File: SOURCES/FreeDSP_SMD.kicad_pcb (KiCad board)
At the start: 2 copper layers, 100 x 100 mm, 169 parts, among them IC1 AD8608, IC2 ADAU1701, IC3 24AA256, IC4 TC7SZ08, IC5 AD8608ARZ, IC6 AD8608, P1 CONN_02X11, P10 CONN_02X10, P2 CONN_2, P3 CONN_02X02, P4 USBi, P5 CONN_02X13, P6 CONN_01X06, P7 CONN_01X06, P8 CONN_01X06, P9 CONN_02X10, Q1 ZXTP25040DFHTA, Q2 2N7000, Q3 2N7000, U1 78033, U2 4040, U3 7805, X1 12M288Hz

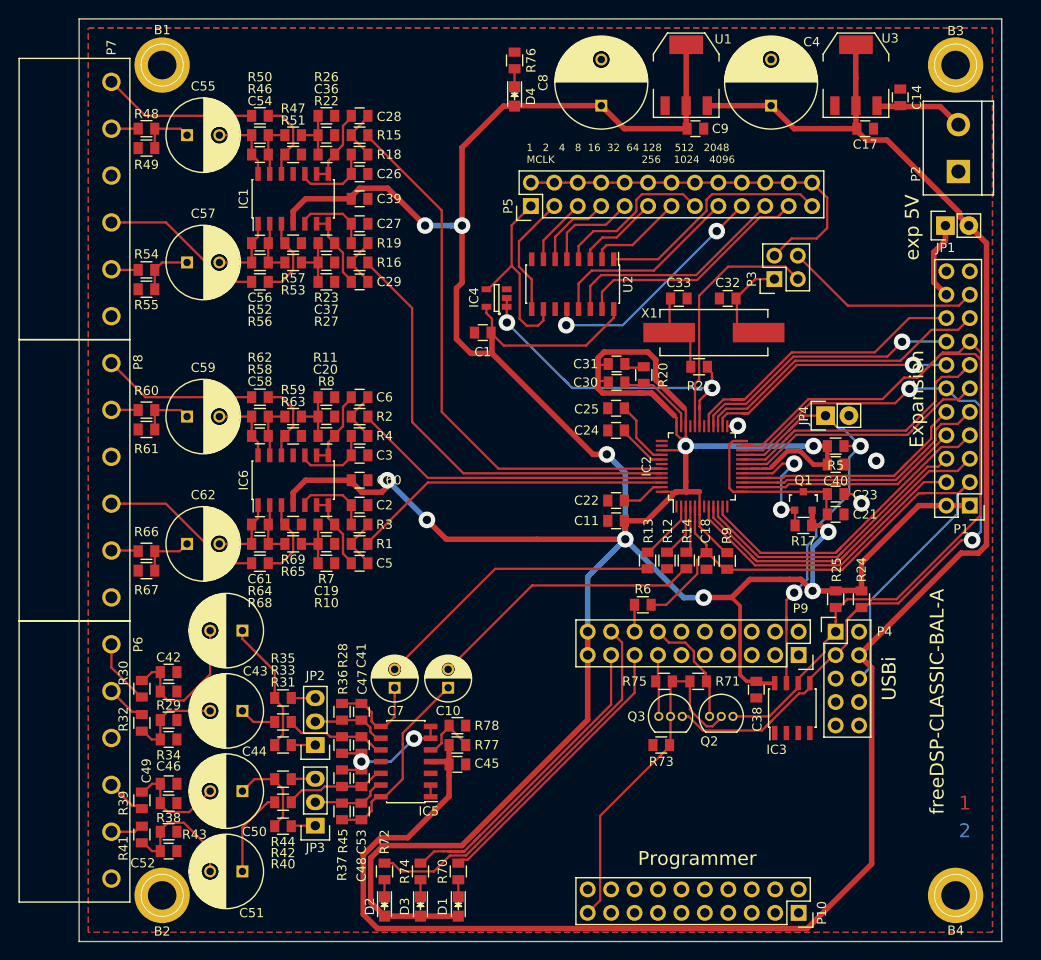
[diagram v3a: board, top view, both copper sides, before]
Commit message: Bugfix DAC-Stage: Applied VCC/2 - Supplied OpAmps with +5V - Reworked gain settings: Pro +6dBu, Consumer -10dBV
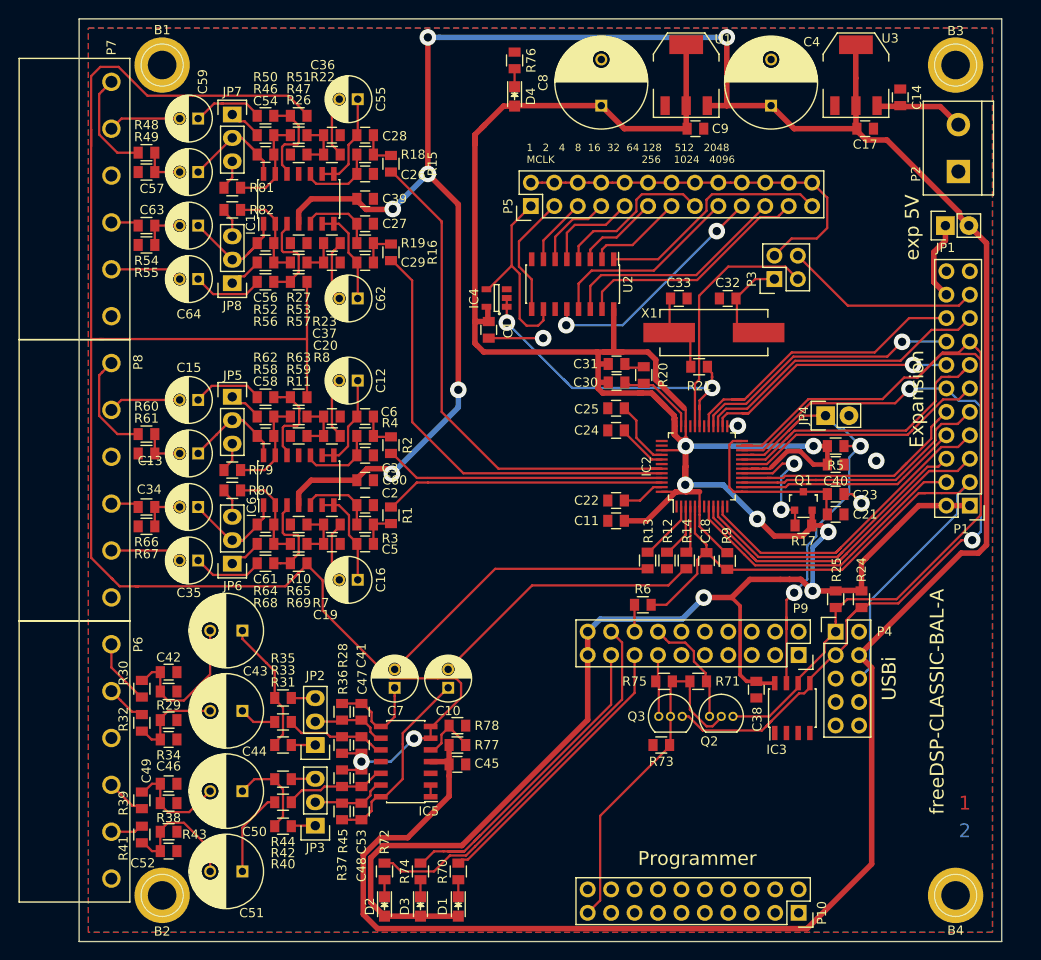
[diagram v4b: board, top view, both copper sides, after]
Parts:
- added C12: 47u0./16V, Capacitors_ThroughHole:C_Radial_D5_L11_P2, F.Cu at (130.2, 89.2)
- added C13: 47u0./16V, Capacitors_ThroughHole:C_Radial_D5_L11_P2, F.Cu at (112.9, 97.1)
- added C15: 47u0./16V, Capacitors_ThroughHole:C_Radial_D5_L11_P2, F.Cu at (112.9, 91.3)
- added C16: 47u0./16V, Capacitors_ThroughHole:C_Radial_D5_L11_P2, F.Cu at (130.2, 110.8)
- added C34: 47u0./16V, Capacitors_ThroughHole:C_Radial_D5_L11_P2, F.Cu at (112.9, 102.9)
- added C35: 47u0./16V, Capacitors_ThroughHole:C_Radial_D5_L11_P2, F.Cu at (112.9, 108.7)
- added C63: 47u0./16V, Capacitors_ThroughHole:C_Radial_D5_L11_P2, F.Cu at (112.9, 72.4)
- added C64: 47u0./16V, Capacitors_ThroughHole:C_Radial_D5_L11_P2, F.Cu at (112.9, 78.2)
- added JP5: JUMPER3, Pin_Headers:Pin_Header_Straight_1x03, F.Cu at (116.6, 91.0)
- added JP6: JUMPER3, Pin_Headers:Pin_Header_Straight_1x03, F.Cu at (116.6, 109.0)
- added JP7: JUMPER3, Pin_Headers:Pin_Header_Straight_1x03, F.Cu at (116.6, 60.4)
- added JP8: JUMPER3, Pin_Headers:Pin_Header_Straight_1x03, F.Cu at (116.6, 78.6)
- added R79: 17K4, rklib:C0805-RES, F.Cu at (116.6, 98.9)
- added R80: 17K4, rklib:C0805-RES, F.Cu at (116.6, 101.1)
- added R81: 17K4, rklib:C0805-RES, F.Cu at (116.6, 68.3)
- added R82: 17K4, rklib:C0805-RES, F.Cu at (116.6, 70.7)
- C55, C57, C59, C62: value 47u0 ./ 35V -> 47u0./16V; footprint Capacitors_ThroughHole:C_Radial_D8_L11.5_P3.5 -> Capacitors_ThroughHole:C_Radial_D5_L11_P2
- IC1, IC6: value AD8608 -> AD8608ARZ
- R10, R11: value 47K0 -> 49K9
- R46, R52, R58, R64: value 10K0 -> 3K57
- R7, R8: value 680R -> 604R
- moved C62 32.4 mm to (130.2, 80.3), turned to 180 degrees
- moved C59 32.3 mm to (112.9, 60.8), turned to 180 degrees
- moved C55 18.9 mm to (130.2, 58.7), turned to 180 degrees
- moved C57 9.87 mm to (112.9, 66.6), turned to 180 degrees
- moved R10 5.16 mm to (123.8, 104.8), turned to 180 degrees
- moved R11 5.16 mm to (123.8, 95.2), turned to 180 degrees
- moved R26 5.16 mm to (123.8, 64.7), turned to 180 degrees
- moved R27 5.16 mm to (123.8, 74.3), turned to 180 degrees
- moved R54 4.80 mm to (107.3, 72.4)
- moved R55 4.80 mm to (107.3, 74.5)
- moved R66 4.80 mm to (107.3, 102.9)
- moved R67 4.80 mm to (107.3, 105.0)
- moved R1 4.60 mm to (133.8, 103.8), turned to 90 degrees
- moved R2 4.60 mm to (133.8, 96.2), turned to 270 degrees
- moved R15 4.60 mm to (133.8, 65.7), turned to 270 degrees
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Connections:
- C39 pad 2: 3V3 -> +5V
- C5 pad 1: Net-(C5-Pad1) -> Net-(C16-Pad1)
- C55 pad 1: Net-(C55-Pad1) -> Net-(C28-Pad1)
- C55 pad 2: Net-(C54-Pad1) -> Net-(C55-Pad2)
- C57 pad 1: Net-(C57-Pad1) -> Net-(C54-Pad1)
- C57 pad 2: Net-(C56-Pad1) -> Net-(C57-Pad2)
- C58 pad 1: Net-(C58-Pad1) -> Net-(C13-Pad1)
- C59 pad 2: Net-(C58-Pad1) -> /OUT1-
- C6 pad 1: Net-(C6-Pad1) -> Net-(C12-Pad1)
- C60 pad 2: 3V3 -> +5V
- C61 pad 1: Net-(C61-Pad1) -> Net-(C34-Pad1)
- C62 pad 1: Net-(C62-Pad1) -> Net-(C29-Pad1)
- C62 pad 2: Net-(C61-Pad1) -> Net-(C62-Pad2)
- IC1 pad 4: 3V3 -> +5V
- IC6 pad 1: Net-(C61-Pad1) -> Net-(C34-Pad1)
- IC6 pad 14: Net-(C58-Pad1) -> Net-(C13-Pad1)
- IC6 pad 4: 3V3 -> +5V
- IC6 pad 6: Net-(C5-Pad1) -> Net-(C16-Pad1)
- IC6 pad 7: Net-(C5-Pad1) -> Net-(C16-Pad1)
- IC6 pad 8: Net-(C6-Pad1) -> Net-(C12-Pad1)
- IC6 pad 9: Net-(C6-Pad1) -> Net-(C12-Pad1)
- P10 pad 1: /PD3 -> (no net)
- P10 pad 10: /PA4 -> (no net)
- P10 pad 11: /USB_COUT -> (no net)
- P10 pad 12: /~USB_CLATCH1 -> (no net)
- P10 pad 13: /CTL2 -> (no net)
- P10 pad 14: /USB_CDATA -> (no net)
- P10 pad 15: /CTL0 -> (no net)
- P10 pad 16: /CTL1 -> (no net)
- P10 pad 17: /PB6 -> (no net)
- P10 pad 18: /PB7 -> (no net)
- P10 pad 2: /PD4 -> (no net)
- P10 pad 20: /PB5 -> (no net)
- P10 pad 3: /PD1 -> (no net)
- P10 pad 4: /PD2 -> (no net)
- P10 pad 5: /USB_CCLK -> (no net)
- P10 pad 6: /PD0 -> (no net)
- P10 pad 7: /PA5 -> (no net)
- P10 pad 8: /PA6 -> (no net)
- P10 pad 9: /PA3 -> (no net)
- P4 pad 2: Net-(P4-Pad2) -> (no net)
- P4 pad 5: Net-(P4-Pad5) -> (no net)
- P4 pad 7: Net-(P4-Pad7) -> (no net)
- P4 pad 8: Net-(P4-Pad8) -> (no net)
- P4 pad 9: Net-(P4-Pad9) -> (no net)
- P7 pad 1: /OUT1- -> /OUT1+
- P7 pad 2: /OUT1+ -> /OUT1-
- P7 pad 4: /OUT2- -> /OUT2+
- P7 pad 5: /OUT2+ -> /OUT2-
- P8 pad 1: /OUT3- -> /OUT3+
- P8 pad 2: /OUT3+ -> /OUT3-
- P8 pad 4: /OUT4- -> /OUT4+
- P8 pad 5: /OUT4+ -> /OUT4-
- P9 pad 1: /PD6 -> (no net)
- P9 pad 11: /IFCLK -> (no net)
- P9 pad 2: /PD5 -> (no net)
- P9 pad 4: /PD7 -> (no net)
- P9 pad 6: /USB_CLK -> (no net)
- P9 pad 7: /RDY1 -> (no net)
- P9 pad 8: /RDY0 -> (no net)
- R22 pad 1: Net-(C28-Pad1) -> Net-(C55-Pad2)
- R23 pad 1: Net-(C29-Pad1) -> Net-(C62-Pad2)
- R46 pad 1: Net-(C54-Pad1) -> Net-(JP7-Pad1)
- R48 pad 2: Net-(C55-Pad1) -> Net-(C57-Pad2)
- R49 pad 1: Net-(C55-Pad1) -> Net-(C57-Pad2)
- R50 pad 1: /OUT1- -> Net-(C59-Pad1)
- R51 pad 2: GND -> /Vcom
- R52 pad 1: Net-(C56-Pad1) -> Net-(JP8-Pad1)
- R54 pad 2: Net-(C57-Pad1) -> Net-(C63-Pad2)
- R55 pad 1: Net-(C57-Pad1) -> Net-(C63-Pad2)
- R56 pad 1: /OUT2- -> Net-(C64-Pad1)
- R57 pad 2: GND -> /Vcom
- R58 pad 1: Net-(C58-Pad1) -> Net-(JP5-Pad1)
- R60 pad 2: Net-(C59-Pad1) -> Net-(C13-Pad2)
- R61 pad 1: Net-(C59-Pad1) -> Net-(C13-Pad2)
- R62 pad 1: /OUT3- -> Net-(C15-Pad1)
- R63 pad 1: Net-(IC6-Pad12) -> /Vcom
- R63 pad 2: GND -> Net-(IC6-Pad12)
- R64 pad 1: Net-(C61-Pad1) -> Net-(JP6-Pad1)
- R66 pad 2: Net-(C62-Pad1) -> Net-(C34-Pad2)
- R67 pad 1: Net-(C62-Pad1) -> Net-(C34-Pad2)
- R68 pad 1: /OUT4- -> Net-(C35-Pad1)
- R69 pad 2: GND -> /Vcom
- R7 pad 1: Net-(C5-Pad1) -> Net-(C16-Pad2)
- R8 pad 1: Net-(C6-Pad1) -> Net-(C12-Pad2)
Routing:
- net /Vcom: track 15.8 -> 190.1 mm
- net +5V: track 207.7 -> 330.9 mm, vias 0 -> 6
- net 3V3: track 412.3 -> 336.1 mm, vias 11 -> 7
- net Net-(C34-Pad1): track 0.00 -> 11.1 mm
- net Net-(C13-Pad1): track 0.00 -> 11.1 mm
- net Net-(C16-Pad1): track 0.00 -> 10.8 mm
- net Net-(C12-Pad1): track 0.00 -> 10.8 mm
- net /OUT4-: track 17.9 -> 7.85 mm
- net /OUT2-: track 17.9 -> 7.92 mm
- net /OUT3-: track 16.7 -> 7.85 mm
- net /OUT1-: track 16.7 -> 7.86 mm
- net Net-(C6-Pad1): track 8.60 -> 0.00 mm
- net Net-(C5-Pad1): track 8.60 -> 0.00 mm
- net /OUT3+: track 2.91 -> 11.3 mm
- net /OUT1+: track 2.90 -> 11.3 mm
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
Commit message: Changed DC supply connector to barrel jack
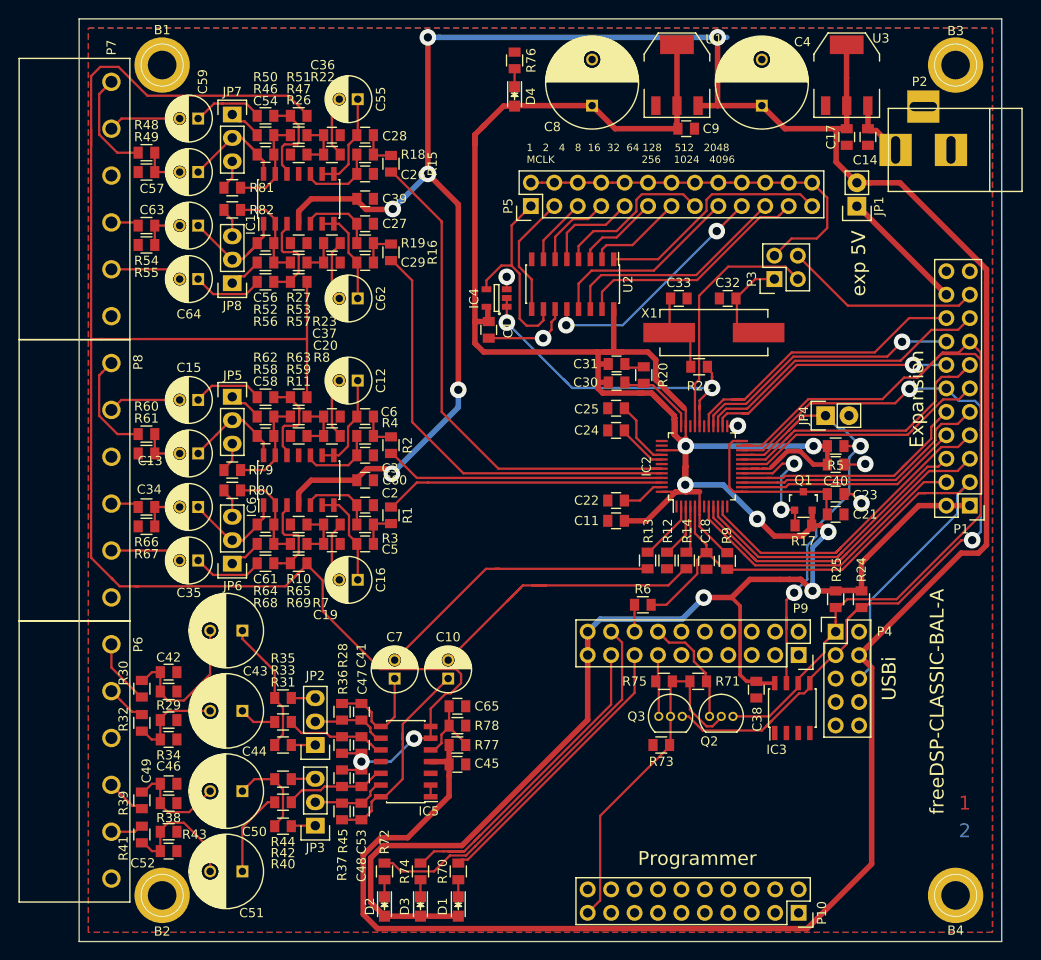
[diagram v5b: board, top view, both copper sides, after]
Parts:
- added C65: 100n, rklib:C0805-X7R, F.Cu at (141.0, 124.5)
- C4, C8: value 220u -> 220u./35V
- P2: value CONN_2 -> BARREL_JACK; footprint Connect:bornier2 -> Connect:BARREL_JACK
- moved JP1 9.83 mm to (184.3, 70.3), turned to 180 degrees
- moved C14 5.54 mm to (185.5, 62.8), turned to 270 degrees
- moved C17 2.19 mm to (183.2, 62.8), turned to 270 degrees
- moved C10 1.00 mm to (140.0, 121.5)
- moved C4 1.00 mm to (174.0, 59.4)
- moved C7 1.00 mm to (134.2, 121.5)
- moved C8 1.00 mm to (155.6, 59.4)
- moved C9 1.00 mm to (165.8, 61.9)
- moved U1 1.00 mm to (164.8, 56.1)
- moved U3 1.00 mm to (183.2, 56.1)
- moved P2 0.63 mm to (194.7, 64.2), turned to 180 degrees
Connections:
- P2 pad 1: GND -> Net-(C14-Pad1)
- P2 pad 2: Net-(C14-Pad1) -> GND
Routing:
- net GND: track 9.38 -> 16.8 mm, vias 3 -> 5
- net Net-(JP1-Pad1): track 8.58 -> 13.7 mm
- net Net-(C14-Pad1): track 9.77 -> 6.46 mm
- net /IN2: track 30.3 -> 33.5 mm
- net +5V: track 330.9 -> 333.4 mm
- net Net-(C65-Pad2): track 6.42 -> 8.52 mm
- net Net-(C10-Pad1): track 20.9 -> 22.6 mm
- net Net-(C41-Pad1): track 10.9 -> 11.9 mm
- net 3V3: track 336.1 -> 335.1 mm
- net /Vcom: track 190.1 -> 191.1 mm
- net Net-(IC4-Pad4): track 21.6 -> 22.3 mm
- net (no net): vias 1 -> 0

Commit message: Moved EZ-USB sockets => EZ-USB now fits into standard enclosure.
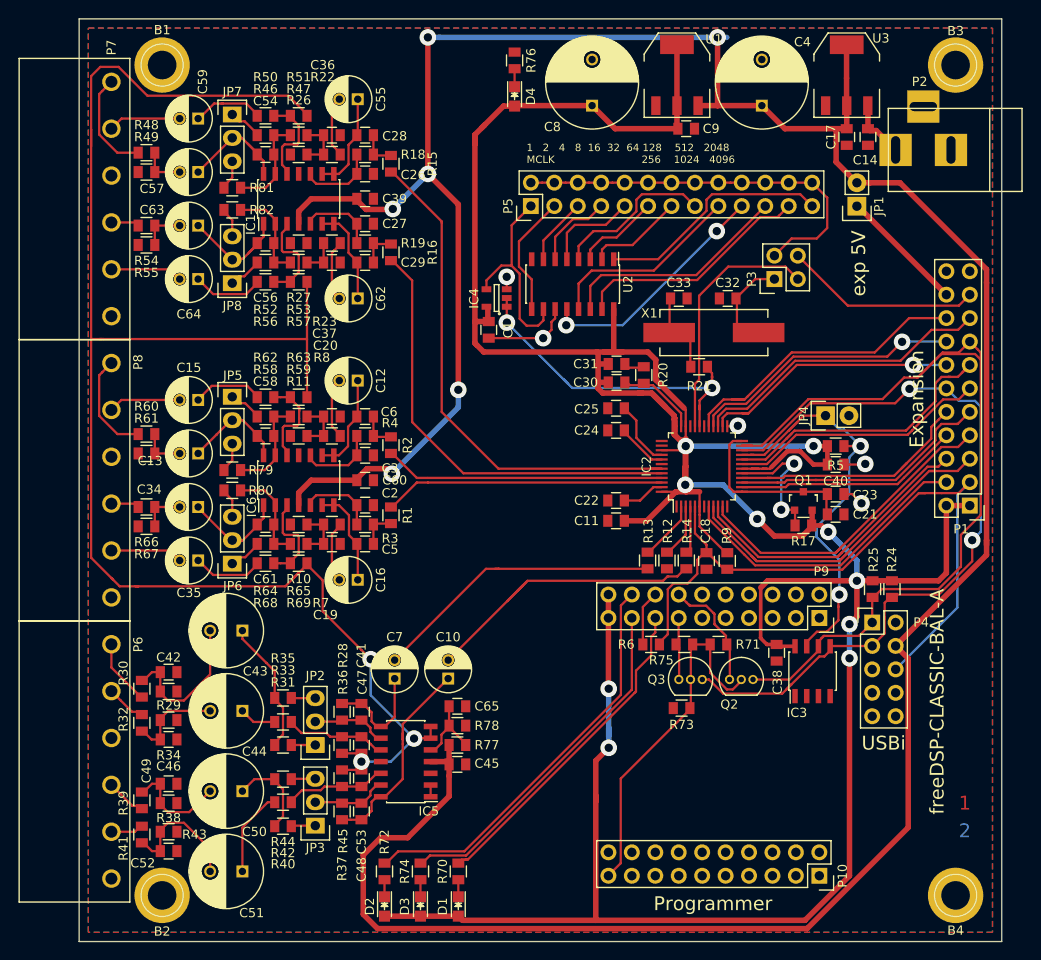
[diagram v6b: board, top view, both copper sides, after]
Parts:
- moved P10 4.61 mm to (180.2, 142.9)
- moved P9 4.61 mm to (180.2, 114.9)
- moved R71 4.57 mm to (169.3, 117.8)
- moved R73 4.57 mm to (165.3, 124.7)
- moved C38 4.57 mm to (175.6, 118.7)
- moved IC3 4.57 mm to (179.5, 120.7)
- moved R75 4.57 mm to (165.6, 117.8)
- moved Q2 4.55 mm to (170.5, 121.6)
- moved Q3 4.55 mm to (165.0, 121.6)
- moved R6 4.39 mm to (162.0, 117.8)
- moved R25 4.15 mm to (186.0, 111.8)
- moved P4 4.08 mm to (186.0, 115.4)
- moved R24 3.48 mm to (188.1, 111.8)
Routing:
- net 3V3: track 335.1 -> 377.9 mm, vias 7 -> 10
- net /Vcom: track 191.1 -> 183.8 mm, vias 2 -> 3
- net /USB_LED1: track 31.0 -> 36.0 mm
- net SDA: track 89.7 -> 86.1 mm
- net Net-(P9-Pad16): track 2.91 -> 5.97 mm
- net /USB_LED2: track 41.8 -> 44.5 mm
- net /WP: track 49.7 -> 47.2 mm
- net /USB_LED3: track 36.6 -> 38.5 mm
- net _RESET: track 74.9 -> 76.7 mm
- net SCL: track 96.4 -> 94.9 mm
- net +5V: track 333.4 -> 332.8 mm

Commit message: Changed expansion header to new standard i2s expansion header
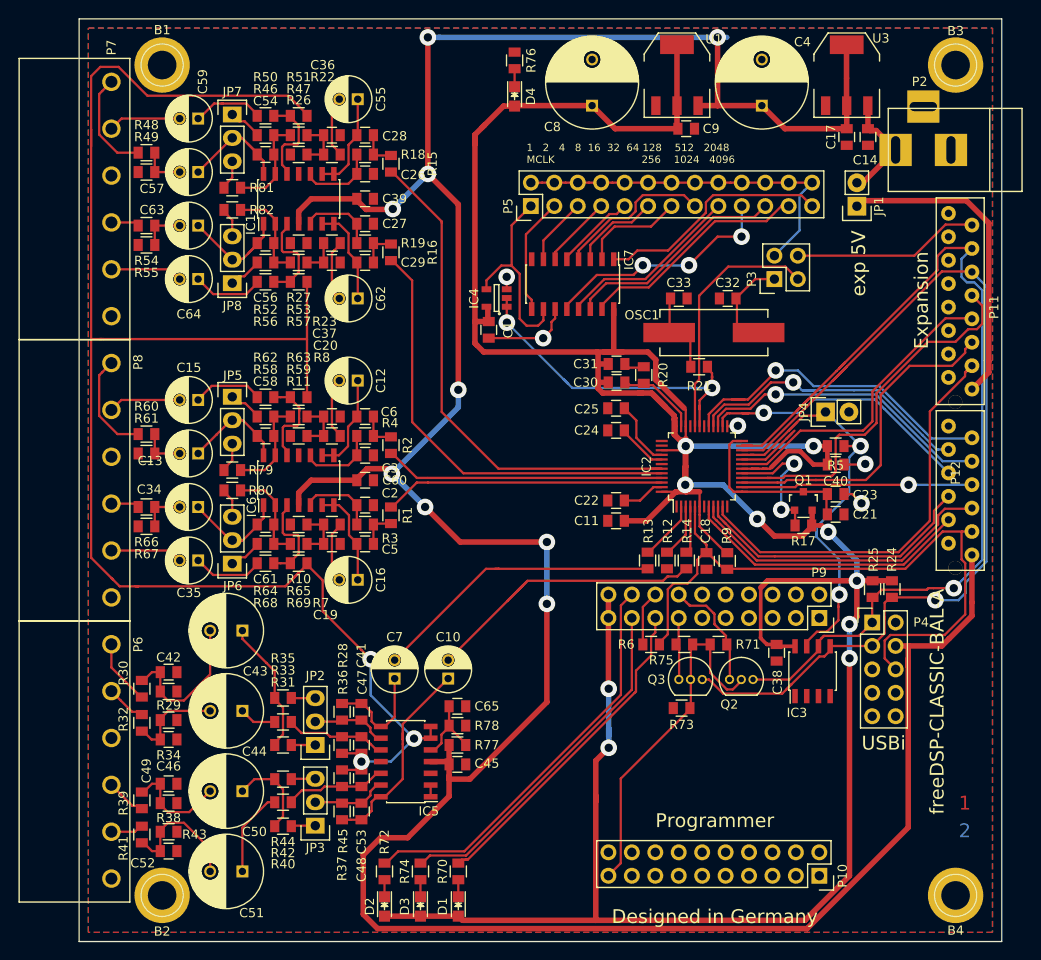
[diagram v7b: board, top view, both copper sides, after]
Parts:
- removed P1: CONN_02X11, Pin_Headers:Pin_Header_Straight_2x11
- removed U2: 4040, Housings_SOIC:SOIC-16_3.9x9.9mm_Pitch1.27mm
- added IC7: 74HC4040D, Housings_SOIC:SOIC-16_3.9x9.9mm_Pitch1.27mm, F.Cu at (153.5, 78.8)
- added P11: MM-16G, rklib:MM-16G, F.Cu at (195.5, 80.6)
- added P12: MM-12G, rklib:MM-12G, F.Cu at (195.5, 101.1)
- IC4: value TC7SZ08 -> SN74LVC1G08DBVR
- moved JP4 0.40 mm to (180.9, 92.6)
- renumbered X1 to OSC1
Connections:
- C10 pad 2: /IN2 -> Net-(C10-Pad2)
- C14 pad 1: Net-(C14-Pad1) -> VCC
- C7 pad 2: /IN1 -> Net-(C7-Pad2)
- IC2 pad 2: Net-(IC2-Pad2) -> /IN1
- IC2 pad 20: WB -> (no net)
- IC2 pad 4: Net-(IC2-Pad4) -> /IN2
- JP1 pad 2: +5V -> VCC
- P2 pad 1: Net-(C14-Pad1) -> VCC
- R13 pad 1: /IN1 -> Net-(C7-Pad2)
- R13 pad 2: Net-(IC2-Pad2) -> /IN1
- R14 pad 1: /IN2 -> Net-(C10-Pad2)
- R14 pad 2: Net-(IC2-Pad4) -> /IN2
- U3 pad VI: Net-(C14-Pad1) -> VCC
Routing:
- net Net-(C10-Pad2): track 0.00 -> 33.8 mm
- net WB: track 32.4 -> 0.00 mm
- net Net-(C7-Pad2): track 0.00 -> 31.9 mm
- net /IN2: track 33.8 -> 5.13 mm
- net SDA: track 86.1 -> 112.5 mm, vias 2 -> 1
- net /IN1: track 31.9 -> 6.54 mm
- net Net-(JP1-Pad1): track 13.7 -> 35.4 mm
- net 3V3: track 377.9 -> 361.7 mm
- net MP10: track 27.0 -> 41.9 mm
- net SCL: track 94.9 -> 107.3 mm, vias 0 -> 1
- net VCC: track 0.00 -> 12.1 mm
- net MP0: track 35.5 -> 45.5 mm
- net (no net): track 0.00 -> 7.80 mm
- net MP6: track 28.7 -> 36.2 mm
- net Net-(IC2-Pad2): track 6.54 -> 0.00 mm
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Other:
- board text added: "Designed in Germany"
